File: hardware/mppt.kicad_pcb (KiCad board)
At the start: 2 copper layers, 92 x 92 mm, 33 parts, among them J1 Conn_01x04_Pin, Q2 BC817, Q3 NTR4171PT1G, U1 INA226

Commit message: updated version
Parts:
- added QR*****: http://192.168.4.1, QRCode:ESesp_qr, F.Cu at (58.2, 131.2)
- moved J1 6.90 mm to (75.4, 125.5)
- moved S1 2.51 mm to (57.9, 146.8)
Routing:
- net +3V3: track 13.1 -> 8.25 mm
- net GND: track 30.8 -> 27.2 mm, vias 9 -> 8
- net Button: track 58.6 -> 55.2 mm
- net SDA: track 56.2 -> 55.6 mm
- net SCL: track 56.1 -> 56.3 mm, vias 0 -> 1

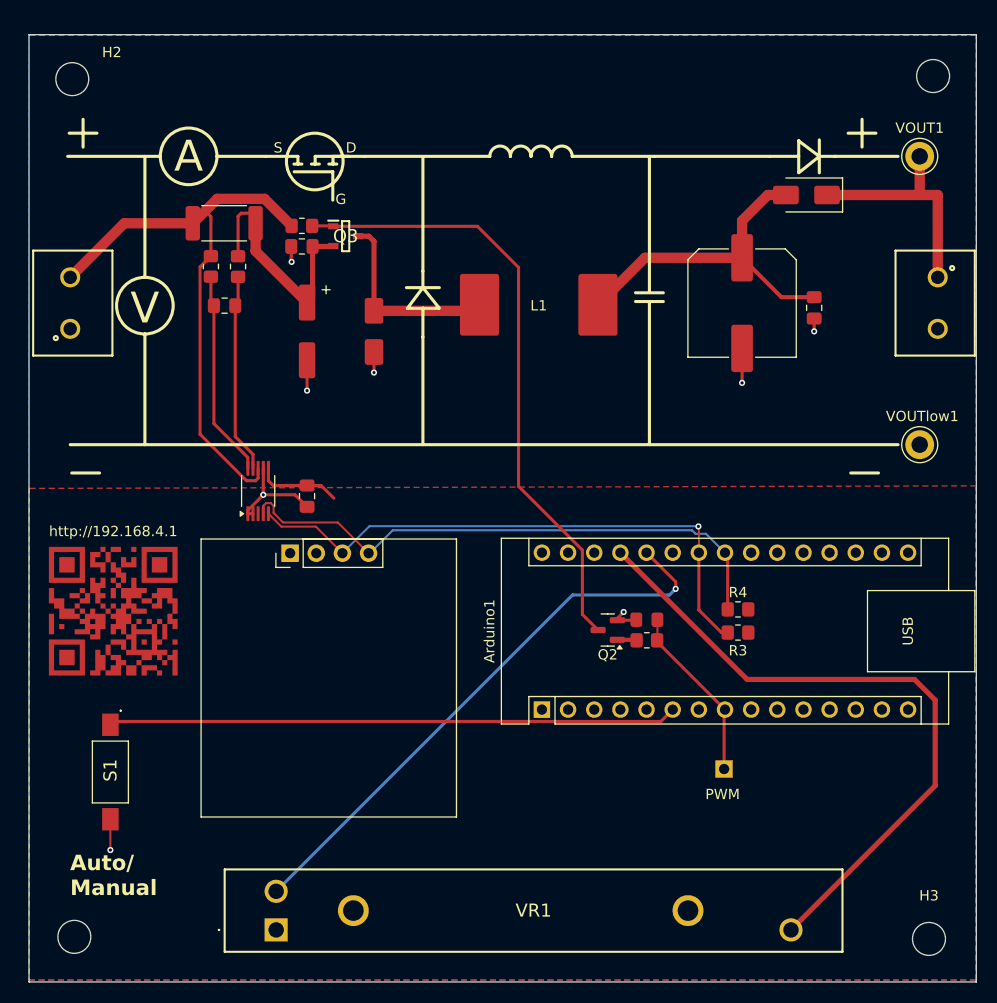
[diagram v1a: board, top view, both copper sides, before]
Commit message: added measurment to output
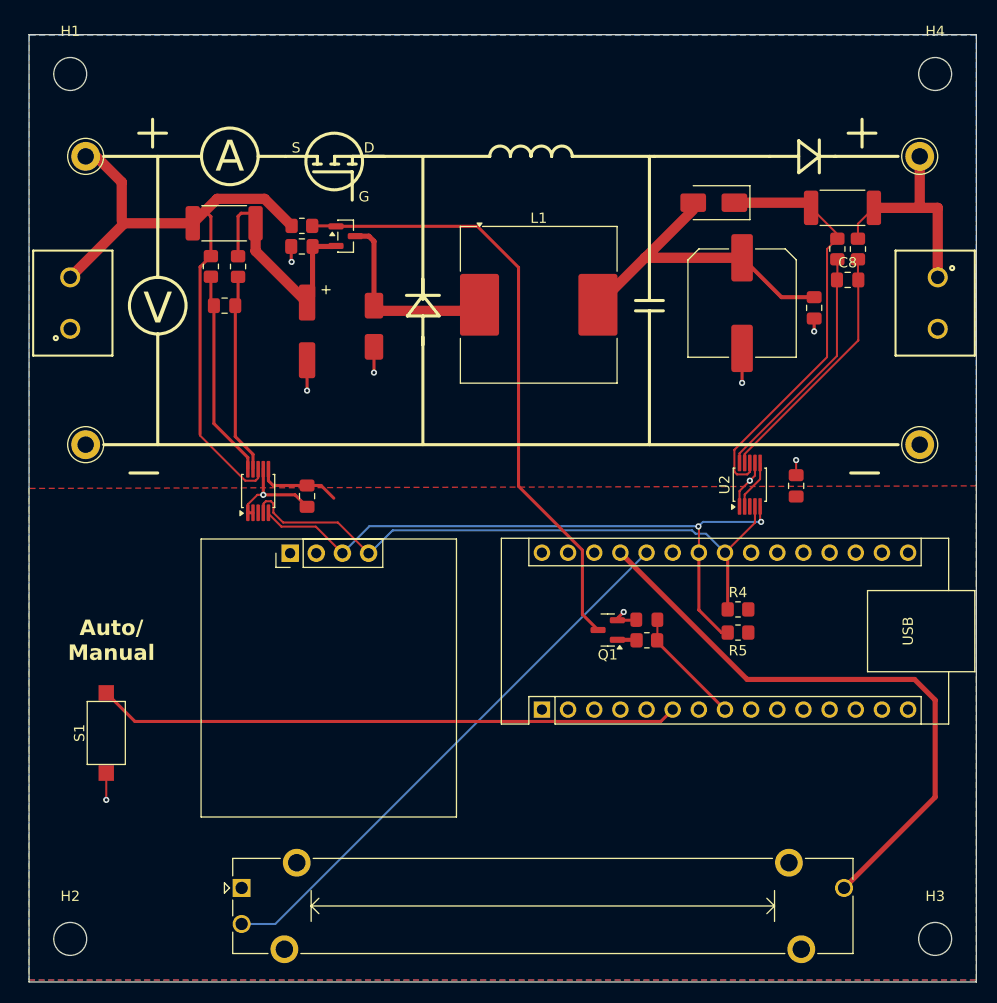
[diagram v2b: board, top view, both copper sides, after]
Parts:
- removed PWM: Conn_01x01_Pin, Connector_PinHeader_2.54mm:PinHeader_1x01_P2.54mm_Vertical
- removed QR*****: http://192.168.4.1, QRCode:ESesp_qr
- removed VR1: RS45111A900F, SamacSys:RS45111A900F
- added C7: 100n, Capacitor_SMD:C_0805_2012Metric_Pad1.18x1.45mm_HandSolder, F.Cu at (124.5, 119.0)
- added C8: 100n, Capacitor_SMD:C_0805_2012Metric_Pad1.18x1.45mm_HandSolder, F.Cu at (129.5, 99.0)
- added R7: 10, Resistor_SMD:R_0805_2012Metric_Pad1.20x1.40mm_HandSolder, F.Cu at (128.5, 96.0)
- added R8: 10, Resistor_SMD:R_0805_2012Metric_Pad1.20x1.40mm_HandSolder, F.Cu at (130.5, 96.0)
- added RV1: R_Potentiometer, Potentiometer_THT:Potentiometer_Bourns_PTA4543_Single_Slide, F.Cu at (70.7, 158.1)
- added Rshunt2: 0.1, Resistor_SMD:R_2512_6332Metric_Pad1.40x3.35mm_HandSolder, F.Cu at (129.0, 92.0)
- added U2: INA226, Package_SO:MSOP-10_3x3mm_P0.5mm, F.Cu at (120.0, 118.9)
- added VIN1: TestPoint, TestPoint:TestPoint_Keystone_5005-5009_Compact, F.Cu at (55.5, 87.0)
- added VIN2: TestPoint, TestPoint:TestPoint_Keystone_5005-5009_Compact, F.Cu at (55.5, 115.0)
- D2: value SS210 -> SS26
- L1: value 2.2m -> 2.2m ( 690mA)
- Q2: renamed from Q3; footprint SamacSys:SOT96P237X111-3N -> Package_TO_SOT_SMD:SOT-23
- R_Gate1: value 100 ohm -> 100
- S1: value 1437566-3 -> BZCN TSB008A2526A; footprint SamacSys:14375663 -> Button_Switch_SMD:SW_SPST_CK_RS282G05A3
- U1: footprint Package_SO:VSSOP-10_3x3mm_P0.5mm -> Package_SO:MSOP-10_3x3mm_P0.5mm
- moved H4 118.4 mm to (138.0, 79.0)
- moved H1 83.8 mm to (54.0, 79.0)
- moved H2 83.5 mm to (54.0, 163.0)
- moved D2 9.03 mm to (116.5, 91.5)
- moved S1 3.81 mm to (57.5, 143.0), turned to 90 degrees
- moved H3 0.60 mm to (138.0, 163.0)
- moved D1 0.50 mm to (83.5, 103.5)
- renumbered Q2 to Q1, R6 to R3, R3 to R5, R5 to R6, RsenseIN1 to Rshunt1
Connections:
- S1 pad 1: Button -> GND
- S1 pad 2: GND -> Button
- VOUT1 pad 1: Net-(D2-K) -> Net-(R8-Pad1)
- VOUT2 pad 1: Net-(D2-K) -> Net-(R8-Pad1)
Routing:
- net Net-(U2-Vin-): track 0.00 -> 24.4 mm
- net Net-(U2-Vin+): track 0.00 -> 23.7 mm
- net Net-(R8-Pad1): track 0.00 -> 21.6 mm
- net Net-(D2-K): track 22.5 -> 41.1 mm
- net SCL: track 56.3 -> 64.1 mm, vias 1 -> 2
- net Net-(U1-Vbus): track 57.8 -> 65.1 mm
- net GND: track 27.2 -> 33.6 mm, vias 8 -> 10
- net SDA: track 55.6 -> 61.7 mm
- net +5V: track 64.6 -> 58.7 mm
- net GatePWM: track 17.4 -> 11.6 mm
- net +3V3: track 8.25 -> 13.1 mm
- net Net-(D2-A): track 33.4 -> 31.1 mm
- net Button: track 55.2 -> 56.6 mm
- net Poti: track 55.6 -> 54.3 mm, vias 1 -> 0

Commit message: added output measurements and adjusted components
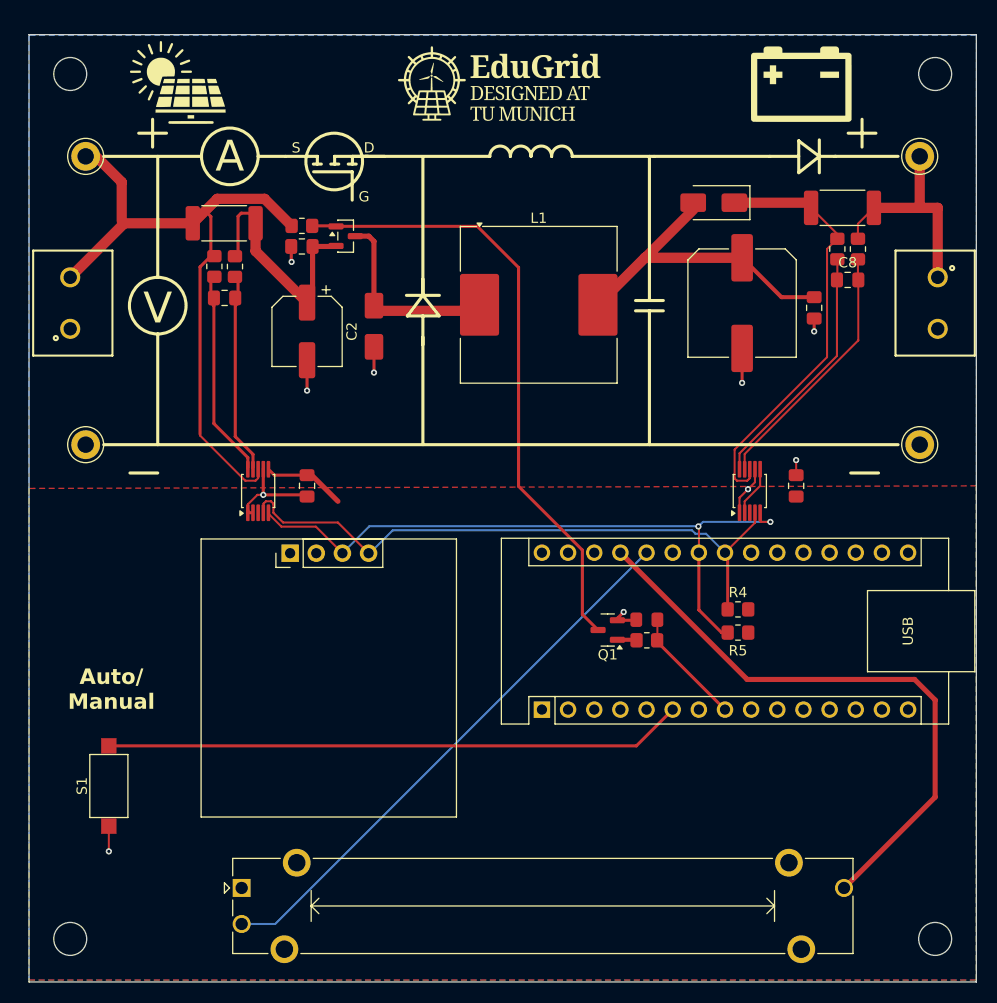
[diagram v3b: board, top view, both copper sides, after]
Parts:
- added G***: LOGO, LOGO, F.Cu at (64.5, 80.0)
- added G***: LOGO, LOGO, F.Cu at (125.0, 80.0)
- added G***: LOGO, LOGO, F.Cu at (95.8, 80.0)
- C2: footprint Capacitor_SMD:CP_Elec_6.3x5.9 -> Capacitor_SMD:CP_Elec_6.3x5.4
- moved S1 5.16 mm to (57.8, 148.2)
- moved C4 1.00 mm to (77.0, 119.0)
- moved C1 0.75 mm to (69.0, 100.8)
- moved U2 0.61 mm to (120.0, 119.5)
- moved R1 0.34 mm to (68.0, 97.7)
- moved R2 0.30 mm to (70.0, 97.7)
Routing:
- net SCL: track 64.1 -> 65.9 mm
- net Net-(D2-K): track 41.1 -> 42.3 mm
- net GND: track 33.6 -> 33.1 mm

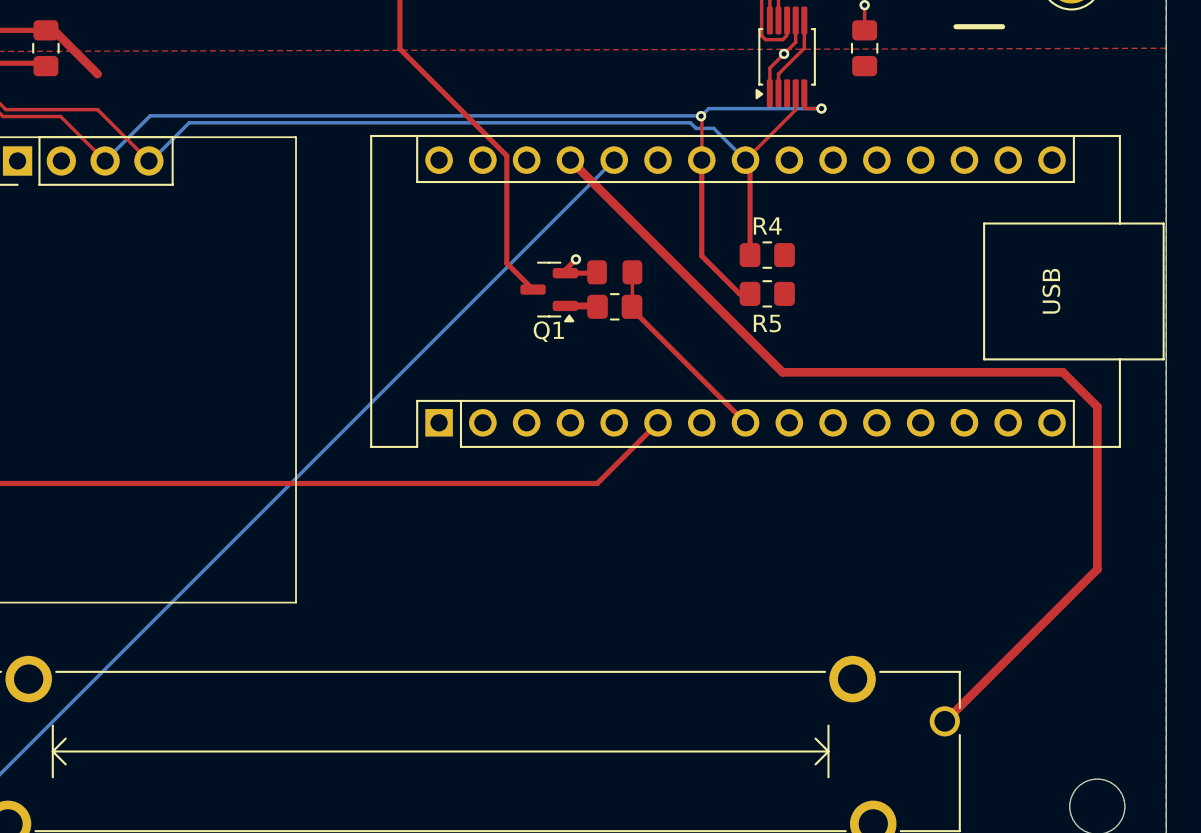
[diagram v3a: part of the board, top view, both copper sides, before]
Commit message: Connected 3.3V instead of 5V to slider poti. This makes the full range available for esp32 and avoids damage to the board
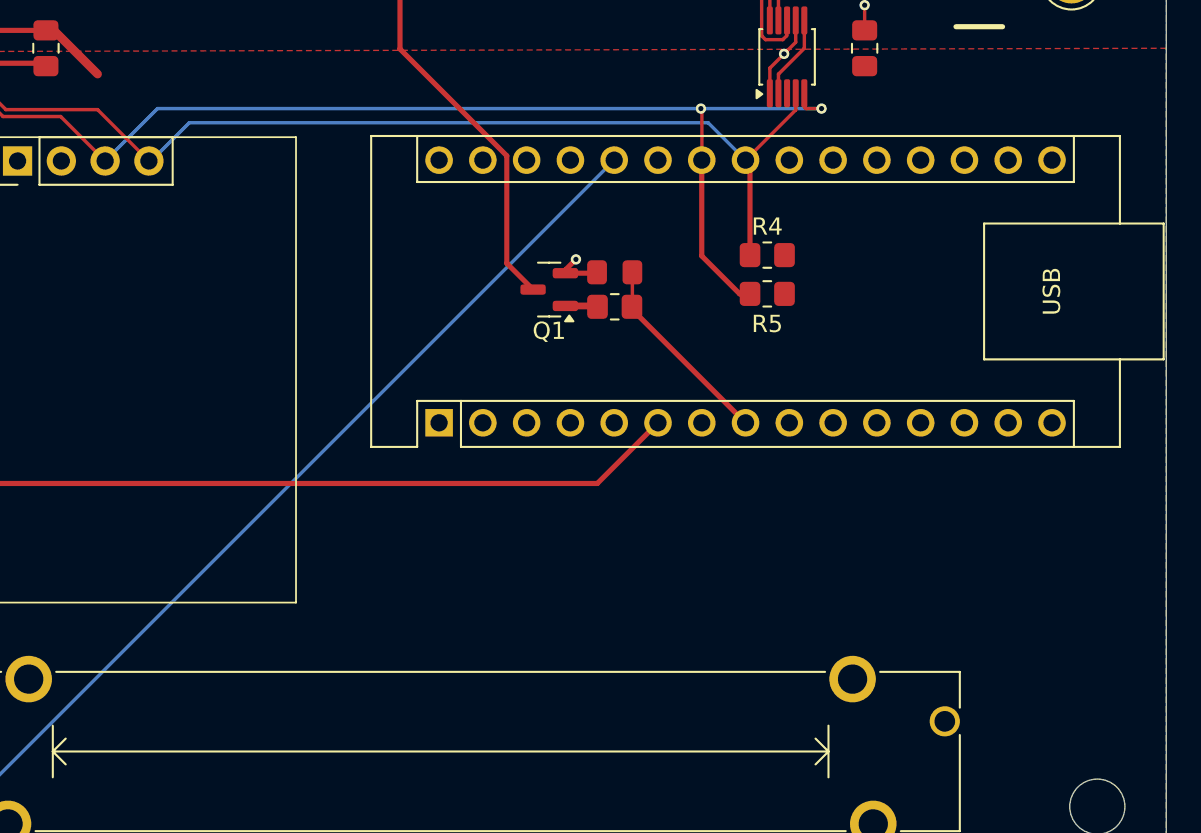
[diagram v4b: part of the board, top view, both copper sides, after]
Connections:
- RV1 pad 3: +5V -> +3V3
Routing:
- net +5V: track 58.7 -> 0.00 mm
